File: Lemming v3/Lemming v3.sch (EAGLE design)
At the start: 37 parts, among them IC1 ADAFRUIT_SENSOR_PCF8574RGY, U1 SIP32431DR3-T1GE3, U2 SIP32431DR3-T1GE3, U3 SIP32431DR3-T1GE3, U4 SIP32431DR3-T1GE3, U5 SIP32431DR3-T1GE3, U6 SIP32431DR3-T1GE3, U7 SIP32431DR3-T1GE3, U8 SIP32431DR3-T1GE3

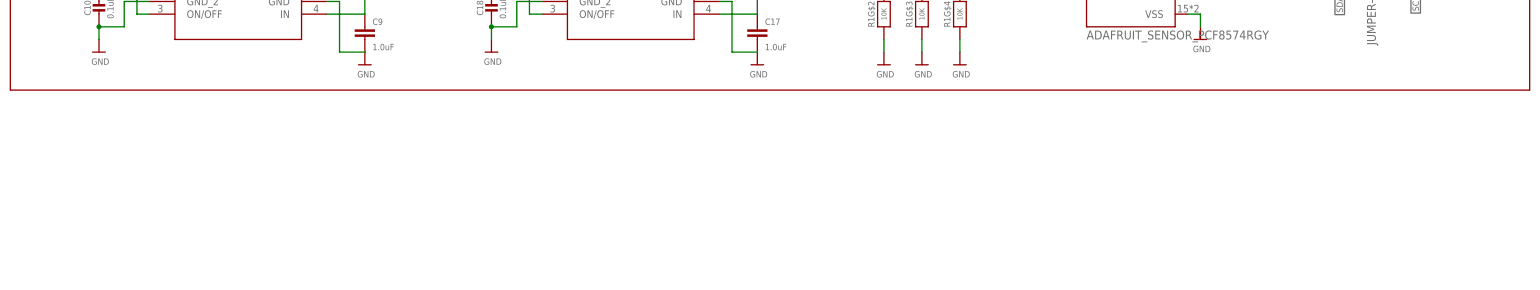
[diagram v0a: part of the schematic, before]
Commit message: Added two more switches with external control
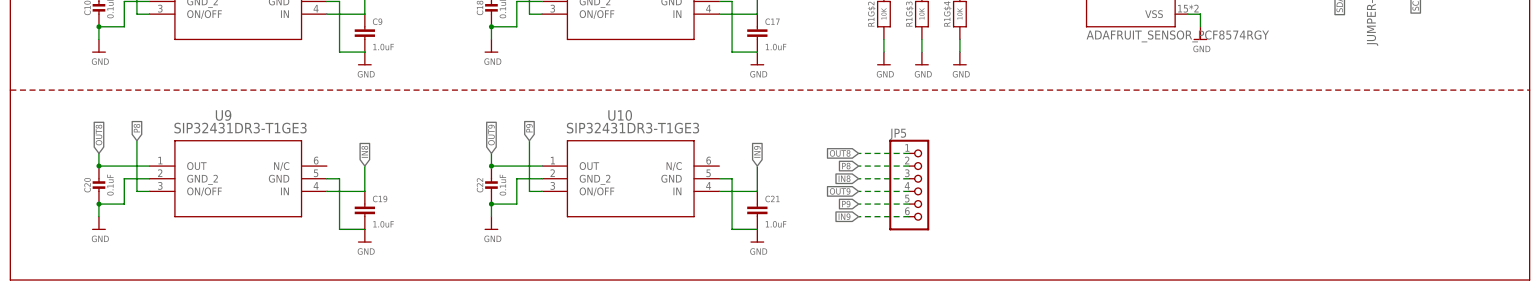
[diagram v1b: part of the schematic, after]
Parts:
- added C19, C21: 1.0uF, SparkFun-Capacitors:1.0UF-0603-16V-10%
- added C20, C22: 0.1uF, microbuilder:CAP_CERAMIC0603_NO
- added JP5: (no value), microbuilder:HEADER-1X670MIL
- added U10, U9: SIP32431DR3-T1GE3, Switch:SIP32431DR3-T1GE3
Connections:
- new net IN8: C19.1, JP5.3, U9.IN
- new net IN9: C21.1, JP5.6, U10.IN
- new net OUT8: C20.1, JP5.1, U9.OUT
- new net OUT9: C22.1, JP5.4, U10.OUT
- new net P8: JP5.2, U9.ON/OFF
- new net P9: JP5.5, U10.ON/OFF
- net GND: now also C19.2, C20.2, C21.2, C22.2, U10.GND, U10.GND_2, U9.GND, U9.GND_2
